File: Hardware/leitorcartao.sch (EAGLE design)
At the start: 158 parts, among them IC1 TL084, IC2 TL084, Q1 BSH103, Q2 BC847ASMD, Q3 BC857ALT1SMD, Q4 BC847ALT1SMD, Q5 BC847ALT1SMD, Q6 BC847ALT1SMD, Q7 BC847ALT1SMD, U1 SAMD20E14A-AUT, U3 TLV1117-50CDCYR, U4 MFRC52202HN1, U5 LP2985-33DBVR, X1 ANTENA 125kHz, X2 MIFARE ANTENA

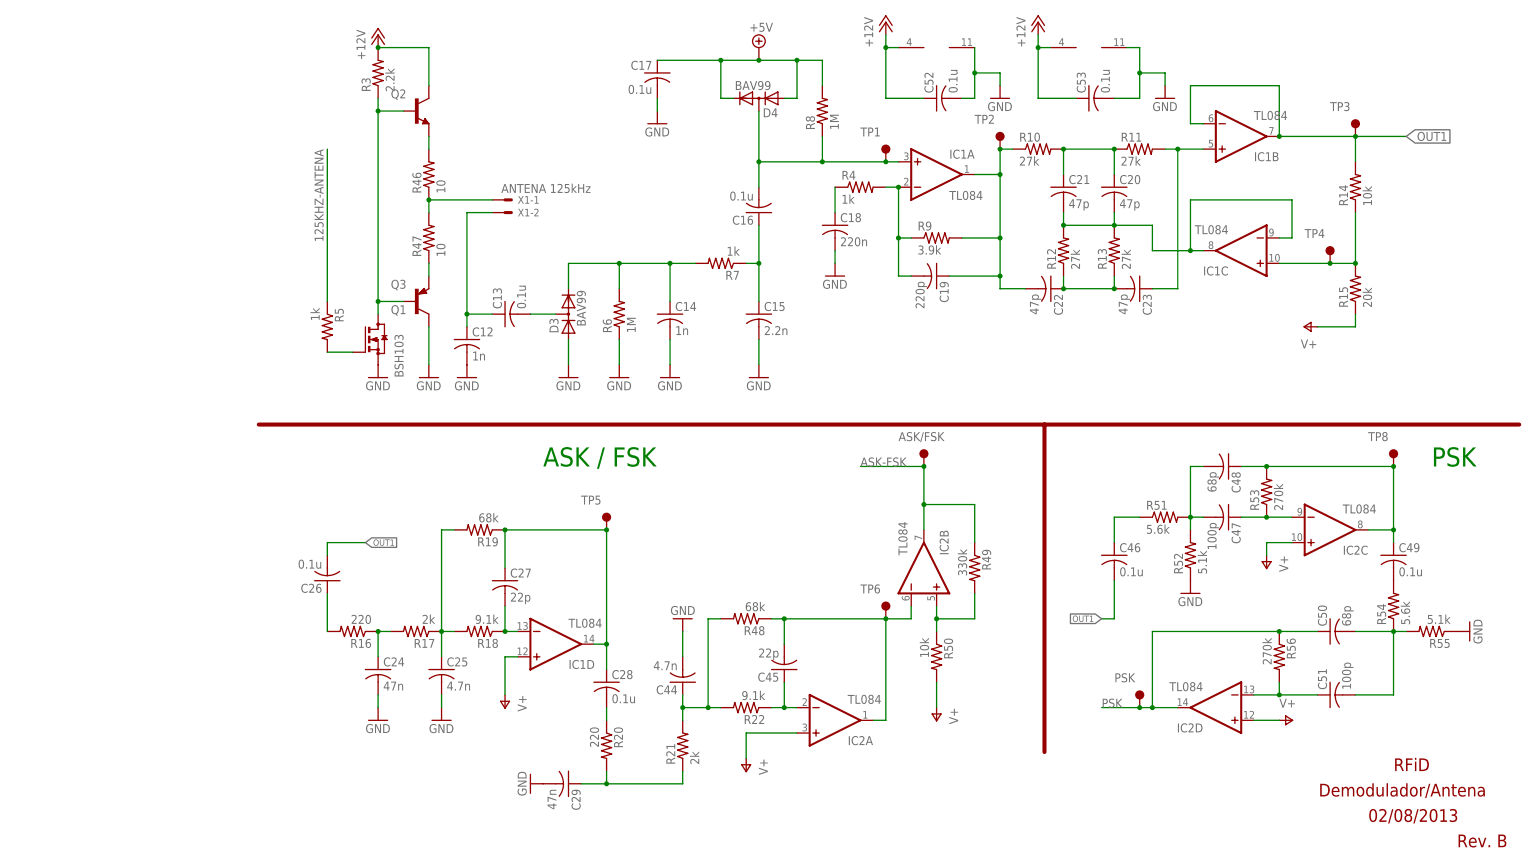
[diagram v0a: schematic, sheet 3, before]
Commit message: Nova versão com as alterações sugeridas por Albert e David.
Componentes da antena do MIFARE alterados para 0603.
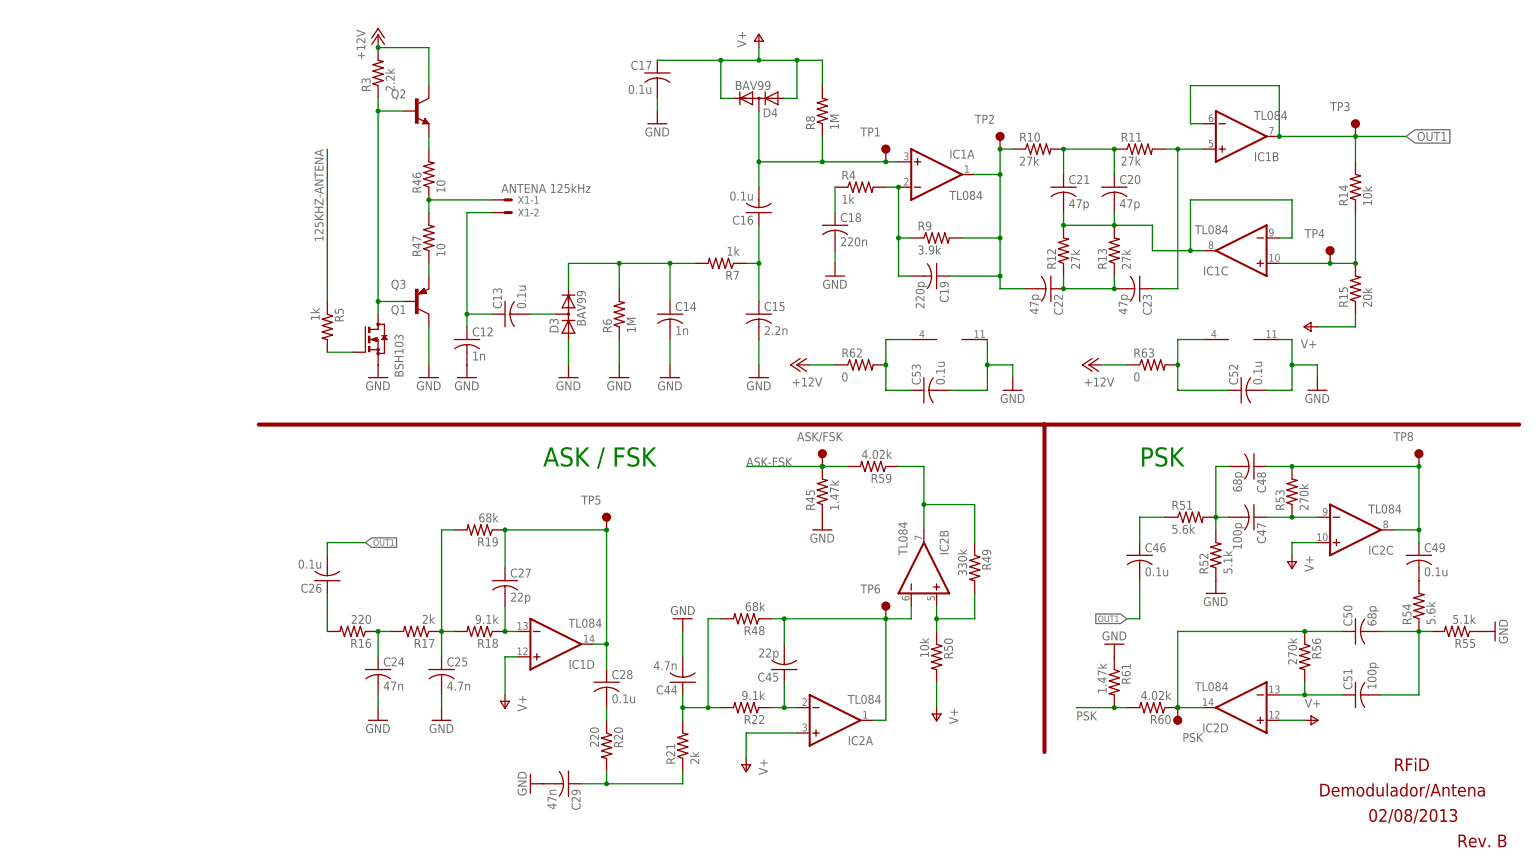
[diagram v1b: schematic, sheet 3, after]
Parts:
- added C56: 10u, RFiD:C-USC0603
- added R45, R61: 1.47k, RFiD:R-US_R0402
- added R59, R60: 4.02k, RFiD:R-US_R0402
- added R62, R63: 0, RFiD:R-US_R0402
- C30, C31: value 0.1u -> 100p
- C34, C35, C36, C37, C38, C39: device RFiD:C-USC0402 -> RFiD:C-USC0603
- R24, R25, R28, R38, R39, R40: device RFiD:R-US_R0402 -> RFiD:R-US_R0603
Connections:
- removed net MIFARE-IRQ: U4B.IRQ
- new net N$40: C50.1, IC2D.OUT, PSK.1, R56.1, R60.1
- new net N$49: C53.1, IC1P.V+, R62.2
- new net N$57: C52.1, IC2P.V+, R63.2
- new net N$90: IC2B.OUT, R49.1, R59.1
- net +12V: now also R62.1, R63.1; no longer C52.1, C53.1, IC1P.V+, IC2P.V+
- net +3V3: now also U4PWR.SVDD
- net +5V: no longer C17.1, D4.1, D4.2, R8.2
- net ASK-FSK: now also R45.2, R59.2; no longer IC2B.OUT, R49.1
- net GND: now also C56.2, R45.1, R61.1; no longer U4PWR.SVDD
- net MIFARE-SCL: now also R2.1, U1IO.PA23; no longer R1.1, U1IO.PA22
- net MIFARE-SDA: now also R1.1, U1IO.PA22; no longer R2.1, U1IO.PA23
- net PSK: now also R60.2, R61.2, U1IO.PA5; no longer C50.1, IC2D.OUT, PSK.1, R56.1
- net V+: now also C17.1, C56.1, D4.1, D4.2, R8.2
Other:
- note added: "PSK - Para uso com Analog Comparator"
- moved on the sheet: ASK/FSK, C32, C33, C46, C47, C48, C49, C50, C51, C52, C53, IC2C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

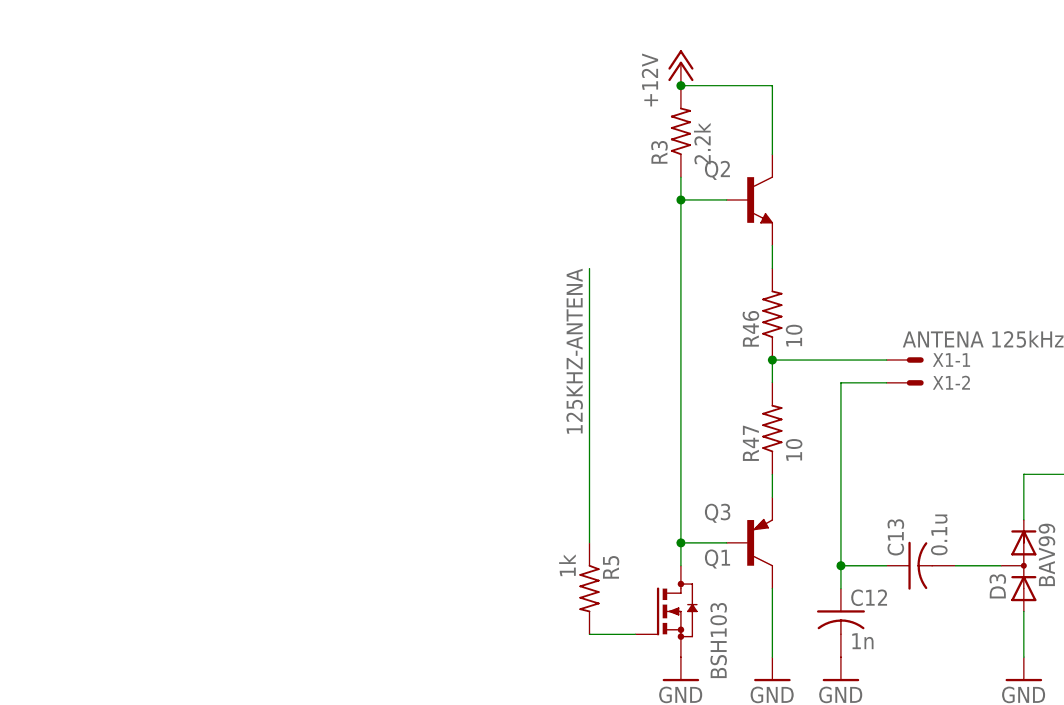
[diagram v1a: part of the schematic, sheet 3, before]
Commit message: Nova versão com a sugestão de um filtro RC na alimentação da antena.
Criado o modelo 3D.
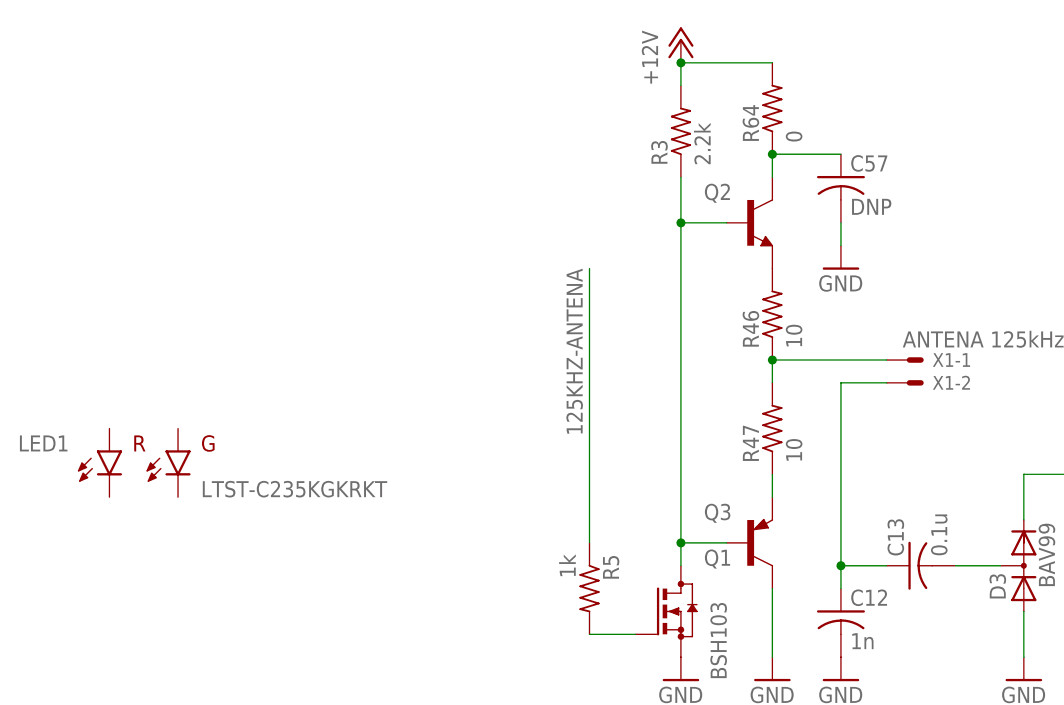
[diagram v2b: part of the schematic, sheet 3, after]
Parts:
- added C57: DNP, RFiD:C-USC0805
- added LED1: LTST-C235KGKRKT, RFiD:LTST-C235KGKRKT
- added R64: 0, RFiD:R-US_R0603
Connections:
- new net N$48: C57.1, Q2.C, R64.1
- net +12V: now also R64.2; no longer Q2.C
- net GND: now also C57.2
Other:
- moved on the sheet: Q2
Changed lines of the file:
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@@
 <part name="C56" library="RFiD" deviceset="C-US" device="C0603" value="10u"/>
 <part name="GND58" library="supply1" deviceset="GND" device=""/>
+<part name="C57" library="RFiD" deviceset="C-US" device="C0805" value="DNP">
+<attribute name="CUSTOMER_PN" value="C/0.1u/50V/C04"/>
+</part>
+<part name="R64" library="RFiD" deviceset="R-US_" device="R0603" value="0">
+<attribute name="CUSTOMER_PN" value="R/1M/5%/04"/>
+</part>
+<part name="GND59" library="supply1" deviceset="GND" device=""/>
+<part name="LED1" library="RFiD" deviceset="LTST-C235KGKRKT" device=""/>
 </parts>
 <sheets>
@@
 <attribute name="CUSTOMER_PN" x="27.94" y="106.68" size="1.778" layer="96" display="off"/>
 </instance>
-<instance part="Q2" gate="G$1" x="35.56" y="152.4" smashed="yes">
-<attribute name="NAME" x="30.48" y="154.94" size="1.778" layer="95"/>
-<attribute name="CUSTOMER_PN" x="35.56" y="152.4" size="1.778" layer="96" display="off"/>
+<instance part="Q2" gate="G$1" x="35.56" y="149.86" smashed="yes">
+<attribute name="NAME" x="30.48" y="152.4" size="1.778" layer="95"/>
+<attribute name="CUSTOMER_PN" x="35.56" y="149.86" size="1.778" layer="96" display="off"/>
 </instance>
 <instance part="Q3" gate="G$1" x="35.56" y="114.3" smashed="yes">
@@
 <attribute name="CUSTOMER_PN" x="116.84" y="152.4" size="1.778" layer="96" display="off"/>
 </instance>
-<instance part="P+4" gate="1" x="27.94" y="167.64"/>
+<instance part="P+4" gate="1" x="27.94" y="170.18"/>
 <instance part="R46" gate="G$1" x="38.1" y="139.7" rot="R90">
 <attribute name="CUSTOMER_PN" x="38.1" y="139.7" size="1.778" layer="96" display="off"/>
@@
 <attribute name="CUSTOMER_PN" x="182.88" y="101.6" size="1.778" layer="96" rot="R270" display="off"/>
 </instance>
+<instance part="C57" gate="G$1" x="45.72" y="154.94">
+<attribute name="CUSTOMER_PN" x="45.72" y="154.94" size="1.778" layer="96" rot="R270" display="off"/>
+</instance>
+<instance part="R64" gate="G$1" x="38.1" y="162.56" rot="R90">
+<attribute name="CUSTOMER_PN" x="38.1" y="162.56" size="1.778" layer="96" display="off"/>
+</instance>
+<instance part="GND59" gate="1" x="45.72" y="144.78"/>
+<instance part="LED1" gate="G$1" x="-30.48" y="121.92"/>
 </instances>
 <busses>
@@
 <wire x1="27.94" y1="111.76" x2="27.94" y2="114.3" width="0.1524" layer="91"/>
 <pinref part="Q2" gate="G$1" pin="B"/>
-<wire x1="27.94" y1="114.3" x2="27.94" y2="152.4" width="0.1524" layer="91"/>
-<wire x1="27.94" y1="152.4" x2="27.94" y2="154.94" width="0.1524" layer="91"/>
-<wire x1="33.02" y1="152.4" x2="27.94" y2="152.4" width="0.1524" layer="91"/>
-<junction x="27.94" y="152.4"/>
+<wire x1="27.94" y1="114.3" x2="27.94" y2="149.86" width="0.1524" layer="91"/>
+<wire x1="27.94" y1="149.86" x2="27.94" y2="154.94" width="0.1524" layer="91"/>
+<wire x1="33.02" y1="149.86" x2="27.94" y2="149.86" width="0.1524" layer="91"/>
+<junction x="27.94" y="149.86"/>
 <pinref part="Q3" gate="G$1" pin="B"/>
 <wire x1="33.02" y1="114.3" x2="27.94" y2="114.3" width="0.1524" layer="91"/>
@@
 <pinref part="R61" gate="G$1" pin="1"/>
 <pinref part="GND56" gate="1" pin="GND"/>
+</segment>
+<segment>
+<pinref part="GND59" gate="1" pin="GND"/>
+<pinref part="C57" gate="G$1" pin="2"/>
+<wire x1="45.72" y1="147.32" x2="45.72" y2="149.86" width="0.1524" layer="91"/>
 </segment>
 </net>
@@
 <pinref part="R3" gate="G$1" pin="2"/>
 <pinref part="P+4" gate="1" pin="+12V"/>
-<pinref part="Q2" gate="G$1" pin="C"/>
-<wire x1="38.1" y1="157.48" x2="38.1" y2="165.1" width="0.1524" layer="91"/>
-<wire x1="38.1" y1="165.1" x2="27.94" y2="165.1" width="0.1524" layer="91"/>
-<junction x="27.94" y="165.1"/>
+<wire x1="27.94" y1="167.64" x2="27.94" y2="165.1" width="0.1524" layer="91"/>
+<pinref part="R64" gate="G$1" pin="2"/>
+<wire x1="27.94" y1="167.64" x2="38.1" y2="167.64" width="0.1524" layer="91"/>
+<junction x="27.94" y="167.64"/>
 </segment>
 <segment>
@@
 <pinref part="Q2" gate="G$1" pin="E"/>
 <pinref part="R46" gate="G$1" pin="2"/>
-<wire x1="38.1" y1="144.78" x2="38.1" y2="147.32" width="0.1524" layer="91"/>
 </segment>
 </net>
@@
 </segment>
 </net>
+<net name="N$48" class="0">
+<segment>
+<pinref part="Q2" gate="G$1" pin="C"/>
+<pinref part="R64" gate="G$1" pin="1"/>
+<wire x1="38.1" y1="154.94" x2="38.1" y2="157.48" width="0.1524" layer="91"/>
+<pinref part="C57" gate="G$1" pin="1"/>
+<wire x1="38.1" y1="157.48" x2="45.72" y2="157.48" width="0.1524" layer="91"/>
+<junction x="38.1" y="157.48"/>
+</segment>
+</net>
